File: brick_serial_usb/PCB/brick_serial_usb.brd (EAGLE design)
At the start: 27.9 x 39.4 mm, 18 parts, among them IC2 FT232RLSSOP

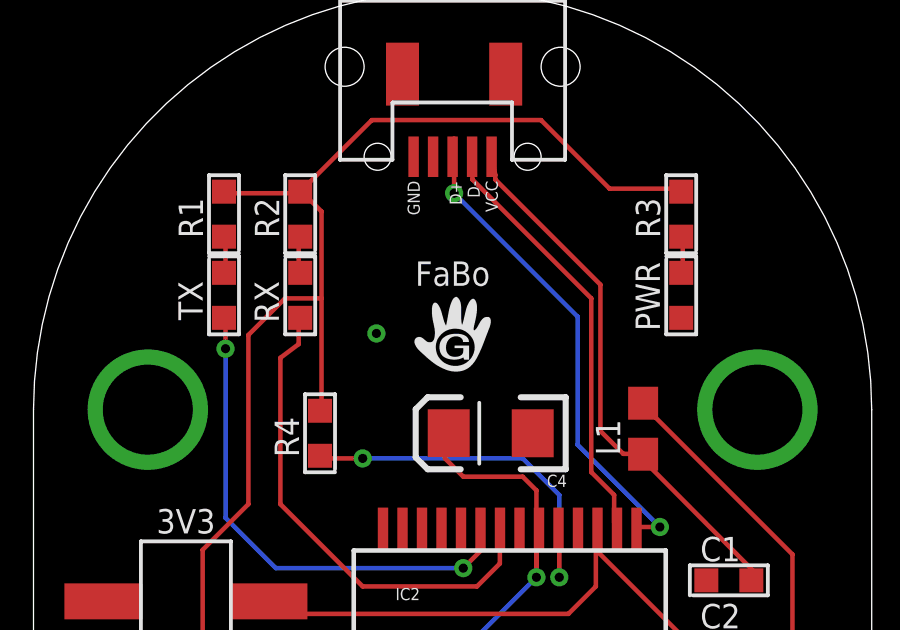
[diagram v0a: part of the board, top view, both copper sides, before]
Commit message: change logo
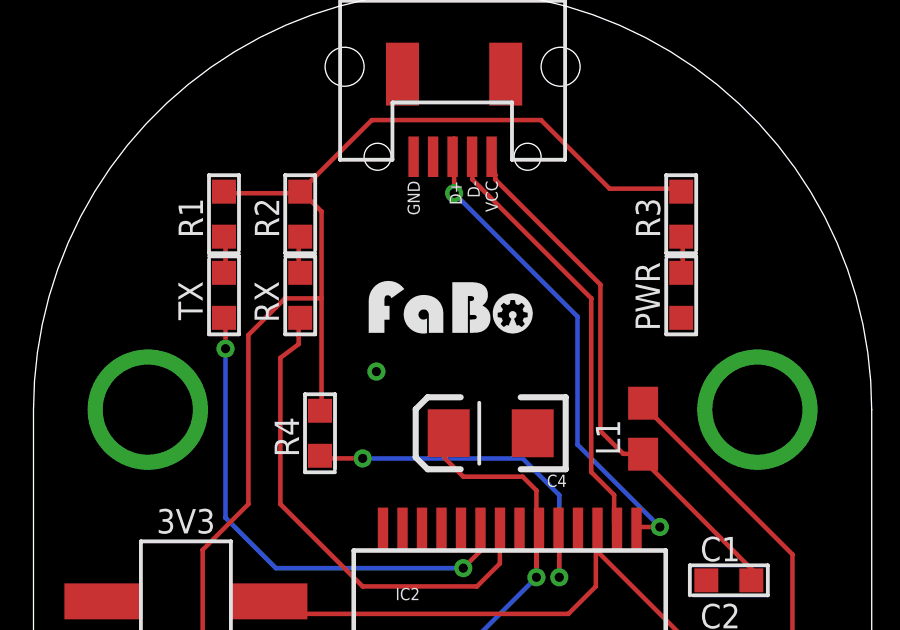
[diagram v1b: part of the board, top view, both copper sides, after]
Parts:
- removed U$4: A4L-LOC-FABO_S, gclue:LOGO_FABO_S
- added U$6: (no value), FaBo:LOGO_FABO_S
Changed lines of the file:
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@@
 <attribute name="NAME" x="22.225" y="15.875" size="0.8128" layer="25" font="vector"/>
 </element>
-<element name="U$4" library="gclue" package="LOGO_FABO_S" value="A4L-LOC-FABO_S" x="13.97" y="27.94"/>
 <element name="U$5" library="gclue" package="LOGO_OSHW_T_S" value="" x="3.81" y="8.89"/>
+<element name="U$6" library="FaBo" package="LOGO_FABO_S" value="" x="13.97" y="27.94"/>
 </elements>
 <signals>
@@
 <vertex x="-1.27" y="40.64"/>
 </polygon>
-<via x="11.43" y="27.94" extent="1-16" drill="0.3048"/>
+<via x="11.43" y="26.67" extent="1-16" drill="0.3048"/>
 </signal>
 <signal name="VCC">

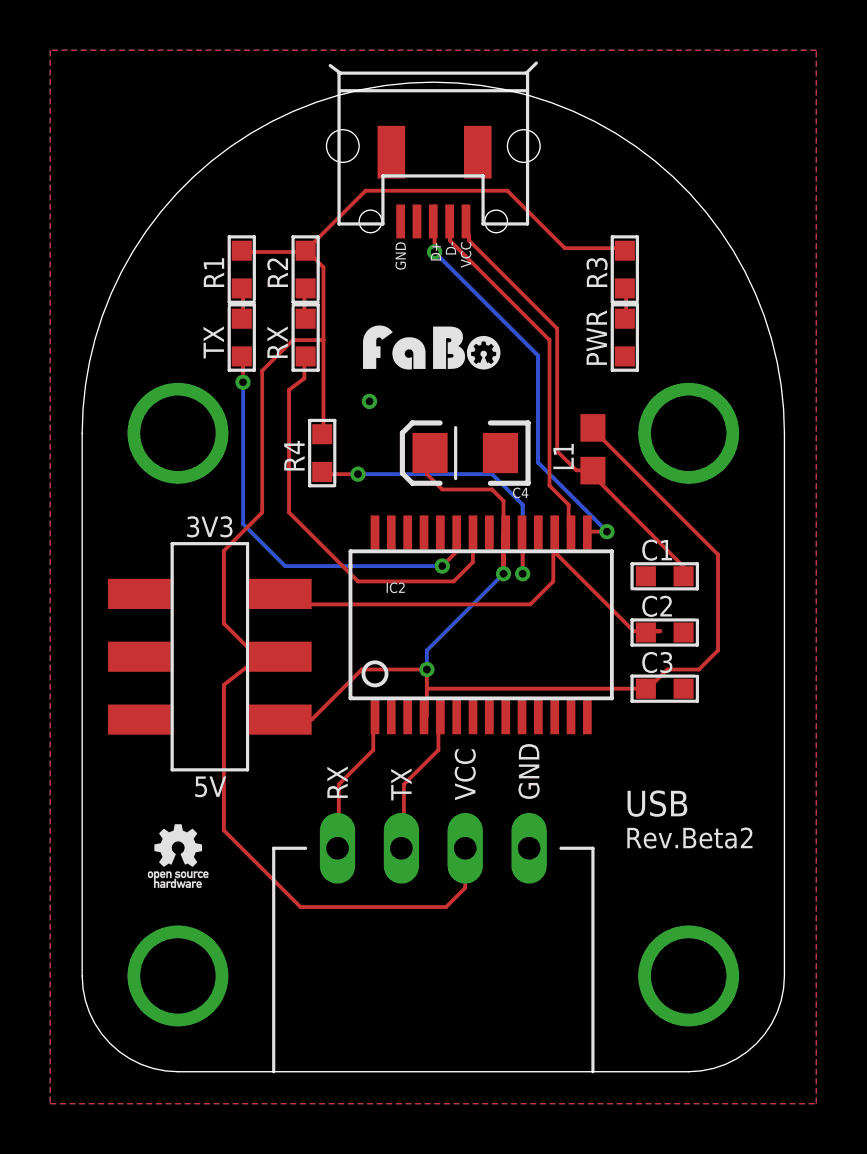
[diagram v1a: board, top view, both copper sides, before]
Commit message: add made-in-japan logo
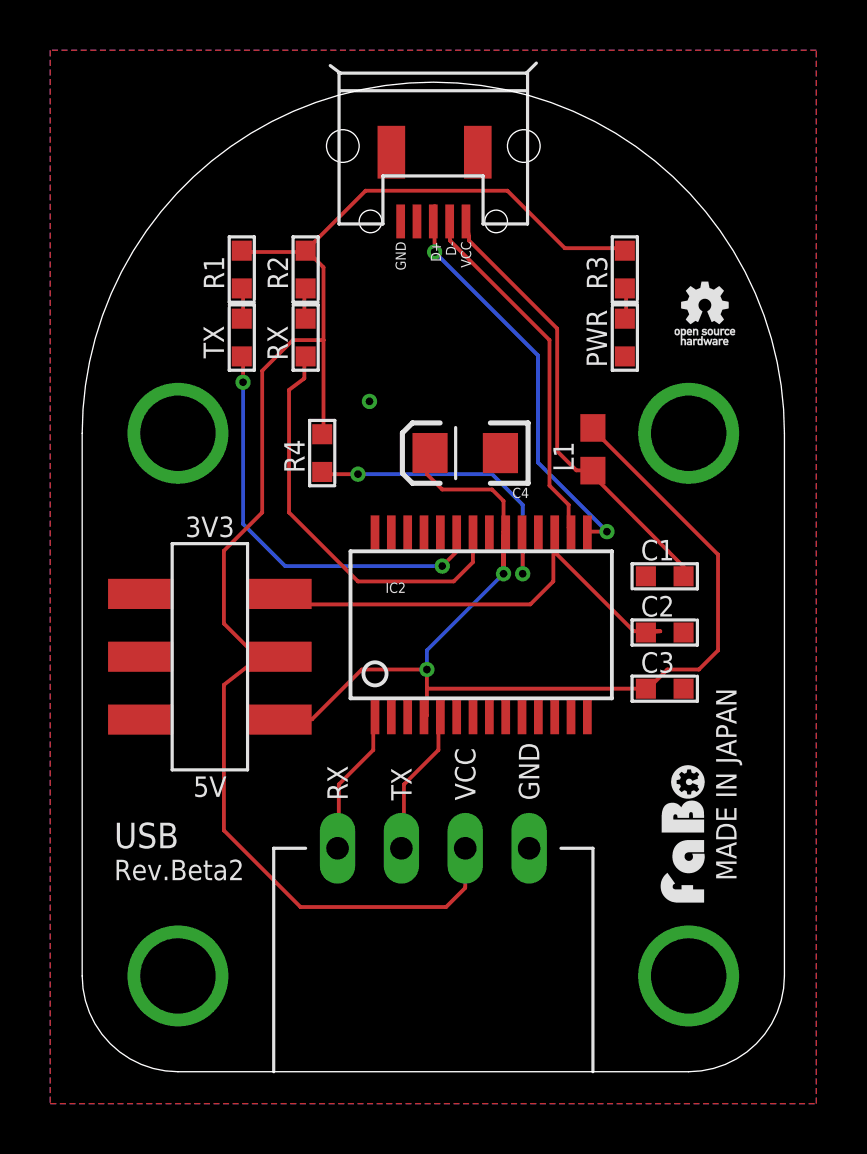
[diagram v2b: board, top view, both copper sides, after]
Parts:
- moved U$5 30.1 mm to (24.8, 30.5)
- moved U$6 21.3 mm to (24.8, 9.53), turned to 90 degrees
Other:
- board text added: "MADE IN JAPAN"
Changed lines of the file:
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@@
 <text x="5.08" y="11.7475" size="0.8128" layer="21" font="vector" align="top-center">5V</text>
 <text x="5.08" y="21.2725" size="0.8128" layer="21" font="vector" align="bottom-center">3V3</text>
-<text x="21.59" y="10.16" size="1.016" layer="21" font="vector">USB</text>
-<text x="21.59" y="8.89" size="0.8128" layer="21" font="vector">Rev.Beta2</text>
+<text x="1.27" y="8.89" size="1.016" layer="21" font="vector">USB</text>
+<text x="1.27" y="7.62" size="0.8128" layer="21" font="vector">Rev.Beta2</text>
+<text x="26.035" y="11.43" size="0.8128" layer="21" font="vector" rot="R90" align="bottom-center">MADE IN JAPAN</text>
 </plain>
 <attributes>
@@
 <attribute name="NAME" x="22.225" y="15.875" size="0.8128" layer="25" font="vector"/>
 </element>
-<element name="U$5" library="gclue" package="LOGO_OSHW_T_S" value="" x="3.81" y="8.89"/>
-<element name="U$6" library="FaBo" package="LOGO_FABO_S" value="" x="13.97" y="27.94"/>
+<element name="U$5" library="gclue" package="LOGO_OSHW_T_S" value="" x="24.765" y="30.48"/>
+<element name="U$6" library="FaBo" package="LOGO_FABO_S" value="" x="24.765" y="9.525" rot="R90"/>
 </elements>
 <signals>

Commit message: Update rev.1.0
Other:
- board text added: "Rev.1.0"
- board text removed: "Rev.Beta2"
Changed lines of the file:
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@@
 <text x="5.08" y="21.2725" size="0.8128" layer="21" font="vector" align="bottom-center">3V3</text>
 <text x="1.27" y="8.89" size="1.016" layer="21" font="vector">USB</text>
-<text x="1.27" y="7.62" size="0.8128" layer="21" font="vector">Rev.Beta2</text>
+<text x="1.27" y="7.62" size="0.8128" layer="21" font="vector">Rev.1.0</text>
 <text x="26.035" y="11.43" size="0.8128" layer="21" font="vector" rot="R90" align="bottom-center">MADE IN JAPAN</text>
 </plain>

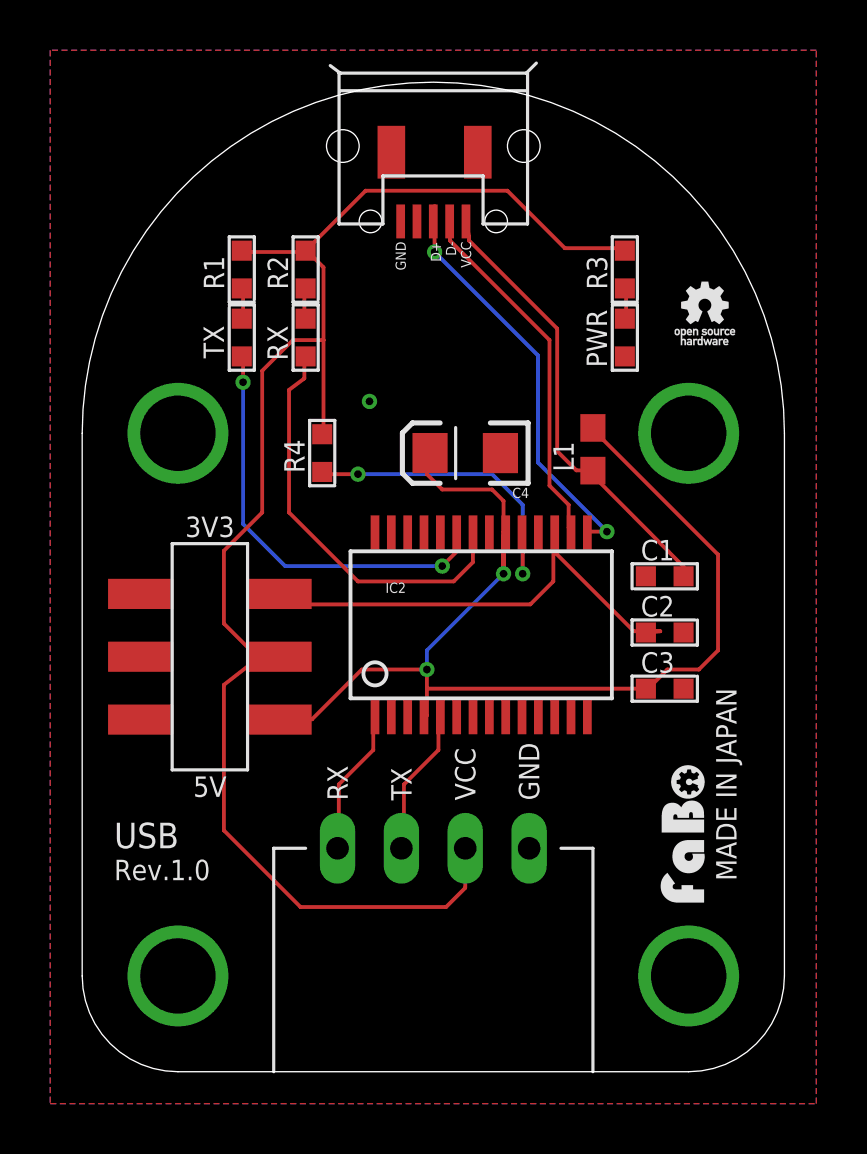
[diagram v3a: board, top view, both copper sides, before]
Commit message: change vcc level  brick_serial_ble_BLE113 refine board  brick_serial_usb
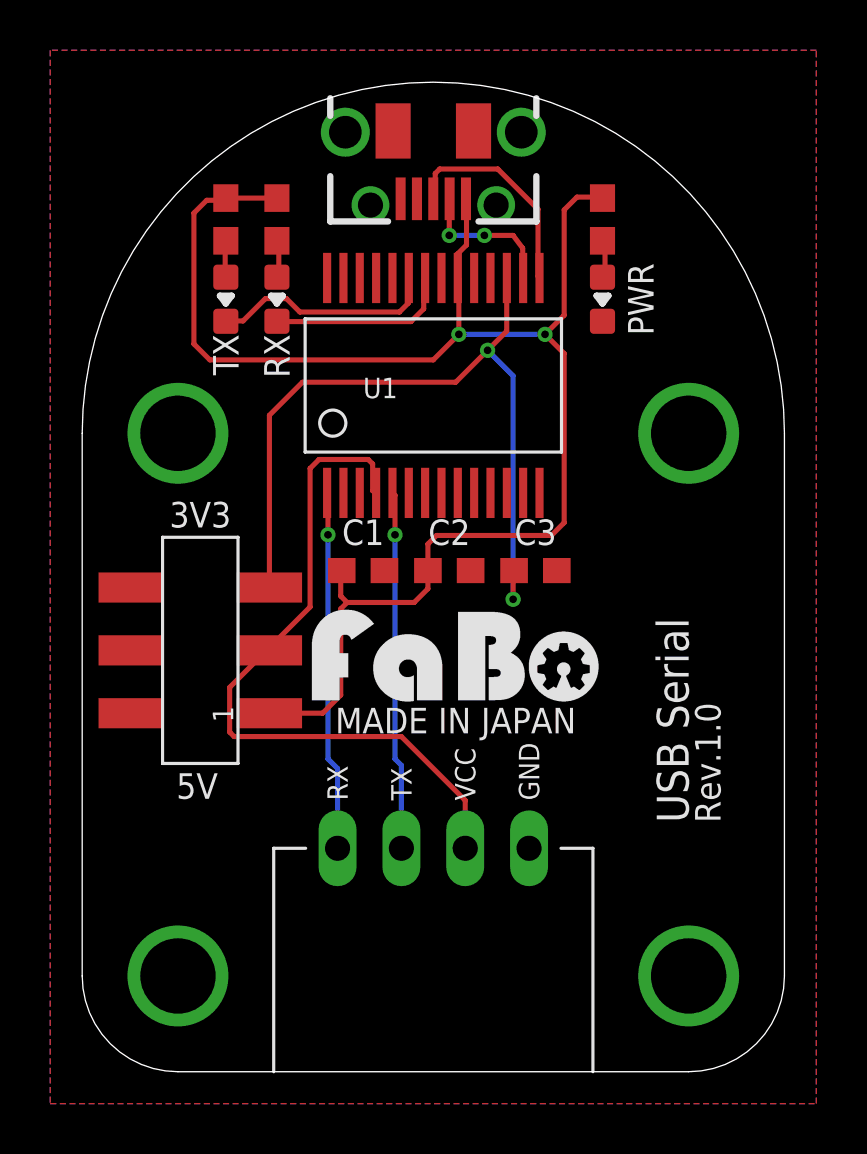
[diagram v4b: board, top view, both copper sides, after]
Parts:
- removed C4: 10μF, SparkFun:EIA3216
- removed IC2: FT232RLSSOP, SparkFun:SSOP28DB
- removed L1: (no value), SparkFun:0603
- removed R4: 4.7K, GClue-Resistors:0603
- removed U$1: USB-MICRO-B-FEMALE, gclue:USB-MICRO-B-FEMALE
- removed U$2: (no value), gclueParts:C&K_JS202011SCQN
- added JP1: USB-B-MICRO_SMD, gclue:USB_B_MICRO
- added SW1: (no value), gclue:C&K_JS202011SCQN
- added U1: FT232RL-SSOP28, gclue:SSOP28
- C1: value 10uf -> 0.1uF; device GClue-Capacitor:0603 -> gclue:EIA0603
- C2: value 0.1uf -> 10uF; device GClue-Capacitor:0603 -> gclue:EIA0603
- C3: value 0.1uf -> 0.1uF; device GClue-Capacitor:0603 -> gclue:EIA0603
- PWR, RX, TX: value LED0603 -> (none); device GClue-LED:0603 -> gclue:EIA0603-LED
- R1, R2, R3: value 270 -> (none); device GClue-Resistors:0603 -> gclue:EIA0603
- U$5: device gclue:LOGO_OSHW_T_S -> FaBo:LOGO_FABO_M
- U$6: device FaBo:LOGO_FABO_S -> gclue:LOGO_OSHW_T_M_BOTTOM
- moved U$5 18.6 mm to (14.9, 14.7)
- moved R1 14.5 mm to (20.7, 33.9)
- moved R3 14.0 mm to (7.75, 33.9)
- moved C1 12.0 mm to (11.2, 19.9)
- moved U$6 11.6 mm to (14.0, 5.33), turned to 0 degrees
- moved C2 8.92 mm to (14.6, 19.9), turned to 0 degrees
- moved C3 6.97 mm to (18.0, 19.9), turned to 0 degrees
- moved R2 3.75 mm to (5.71, 33.9)
- moved RX 1.91 mm to (7.75, 30.7), turned to 180 degrees
- moved PWR 1.76 mm to (20.7, 30.7), turned to 180 degrees
- moved TX 1.65 mm to (5.71, 30.7), turned to 180 degrees
- renumbered U$3 to J1
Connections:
- removed net +3V3: C2.2, IC2.17, U$2.3
- removed net +5V: C3.2, C4.A, IC2.20, IC2.4, L1.2, U$2.1
- removed net CTS: IC2.11
- removed net D+: IC2.15, U$1.D+
- removed net D-: IC2.16, U$1.D-
- removed net DCD: IC2.10
- removed net DSR: IC2.9
- removed net DTR: IC2.2
- removed net N$6: PWR.ANODE, R3.1
- removed net PWREN: IC2.14
- removed net RESET: IC2.19, R4.1
- removed net RI: IC2.6
- removed net RTS: IC2.3
- removed net SLEEP: IC2.12
- removed net TXDEN: IC2.13
- new net 3V3: C3.1, SW1.3, U1.17
- new net 5V: C1.1, C2.1, JP1.VBUS, R1.2, R2.2, R3.2, SW1.1, U1.20
- new net N$3: R3.1, RX.A
- new net N$4: JP1.D-, U1.16
- net GND: now also C1.2, C2.2, C3.2, JP1.GND, PWR.C, U1.18, U1.21, U1.25, U1.26, U1.7; no longer C1.1, C2.1, C3.1, C4.C, IC2.18, IC2.21, IC2.25, IC2.26, IC2.7, PWR.CATHODE, U$1.GND, U$1.GND1, U$1.GND2
- net N$1: now also PWR.A, R1.1; no longer C1.2, L1.1, U$1.VCC
- net N$2: now also R2.1, TX.A; no longer R1.1, TX.ANODE
- net N$5: now also JP1.D+, U1.15; no longer R2.1, RX.ANODE
- net RX: now also J1.RX, U1.1; no longer IC2.5, J1.TX
- net RXLED: now also RX.C, U1.22; no longer IC2.22, RX.CATHODE
- net TX: now also J1.TX, U1.5; no longer IC2.1, J1.RX
- net TXLED: now also TX.C, U1.23; no longer IC2.23, TX.CATHODE
- net VCC: now also SW1.2, U1.4; no longer R1.2, R2.2, R3.2, R4.2, U$2.2
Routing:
- net 5V: track 0.00 -> 63.1 mm, vias 0 -> 2
- net +5V: track 47.8 -> 0.00 mm, vias 2 -> 0
- net VCC: track 61.6 -> 28.2 mm
- net 3V3: track 0.00 -> 31.3 mm, vias 0 -> 2
- net +3V3: track 19.5 -> 0.00 mm
- net N$1: track 18.5 -> 1.55 mm
- net D+: track 16.7 -> 0.00 mm, vias 2 -> 0
- net D-: track 14.4 -> 0.00 mm
- net RESET: track 12.9 -> 0.00 mm, vias 2 -> 0
- net RXLED: track 16.5 -> 7.30 mm
- net TX: track 5.83 -> 14.3 mm, vias 0 -> 1
- net RX: track 5.88 -> 14.3 mm, vias 0 -> 1
- net TXLED: track 16.9 -> 9.00 mm, vias 2 -> 0
- net N$5: track 1.24 -> 8.61 mm
- net N$4: track 0.00 -> 5.82 mm, vias 0 -> 2
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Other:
- board text added: "USB Serial"
- board text removed: "USB"

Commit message: change brick_serial_usb
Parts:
- J1: device gclue:BRICK_SERIAL -> FaBo-etc:BRICK_SERIAL
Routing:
- net 3V3: track 31.3 -> 30.4 mm
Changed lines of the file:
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@@
 </autorouter>
 <elements>
-<element name="J1" library="gclue" package="BRICK_SERIAL" value="" x="13.97" y="19.05"/>
 <element name="U1" library="gclue" package="SSOP28" value="FT232RL-SSOP28" x="13.97" y="27.305" smashed="yes">
 <attribute name="NAME" x="11.176" y="26.797" size="0.8128" layer="25" font="vector"/>
@@
 <element name="U$5" library="FaBo" package="LOGO_FABO_M" value="" x="14.859" y="14.732"/>
 <element name="U$6" library="gclue" package="LOGO_OSHW_T_M_BOTTOM" value="" x="13.97" y="5.334"/>
+<element name="J1" library="FaBo-etc" package="BRICK_SERIAL" value="" x="13.97" y="19.05"/>
 </elements>
 <signals>
@@
 <contactref element="C2" pad="2"/>
 <contactref element="JP1" pad="GND"/>
-<contactref element="J1" pad="GND"/>
 <contactref element="PWR" pad="C"/>
 <polygon width="0.2032" layer="16" spacing="0.1524">
@@
 <vertex x="-1.27" y="40.64"/>
 </polygon>
+<contactref element="J1" pad="GND"/>
 </signal>
 <signal name="5V">
@@
 <contactref element="C3" pad="1"/>
 <contactref element="SW1" pad="3"/>
-<wire x1="7.449" y1="19.264" x2="7.449" y2="26.118" width="0.2032" layer="1"/>
-<wire x1="7.449" y1="26.118" x2="8.763" y2="27.432" width="0.2032" layer="1"/>
-<wire x1="8.763" y1="27.432" x2="14.859" y2="27.432" width="0.2032" layer="1"/>
-<wire x1="14.859" y1="27.432" x2="16.0655" y2="28.6385" width="0.2032" layer="1"/>
-<wire x1="16.129" y1="28.702" x2="16.891" y2="29.464" width="0.2032" layer="1"/>
-<wire x1="16.891" y1="29.464" x2="16.891" y2="31.576" width="0.2032" layer="1"/>
+<wire x1="7.449" y1="19.264" x2="7.449" y2="24.848" width="0.2032" layer="1"/>
+<wire x1="7.449" y1="24.848" x2="9.271" y2="26.67" width="0.2032" layer="1"/>
+<wire x1="9.271" y1="26.67" x2="15.621" y2="26.67" width="0.2032" layer="1"/>
+<wire x1="15.621" y1="26.67" x2="16.891" y2="27.94" width="0.2032" layer="1"/>
+<wire x1="16.891" y1="27.94" x2="16.891" y2="31.576" width="0.2032" layer="1"/>
 <wire x1="16.891" y1="31.576" x2="16.895" y2="31.58" width="0.2032" layer="1"/>
 <wire x1="17.184" y1="19.939" x2="17.184" y2="19.851" width="0.2032" layer="1"/>
@@
 <via x="17.145" y="18.796" extent="1-16" drill="0.3048"/>
 <wire x1="17.145" y1="18.796" x2="17.145" y2="27.686" width="0.2032" layer="16"/>
-<wire x1="17.145" y1="27.686" x2="16.129" y2="28.702" width="0.2032" layer="16"/>
-<via x="16.129" y="28.702" extent="1-16" drill="0.3048"/>
-<wire x1="16.129" y1="28.702" x2="16.0655" y2="28.6385" width="0.2032" layer="1"/>
+<wire x1="17.145" y1="27.686" x2="16.891" y2="27.94" width="0.2032" layer="16"/>
+<via x="16.891" y="27.94" extent="1-16" drill="0.3048"/>
 </signal>
 <signal name="VCC">
 <contactref element="U1" pad="4"/>
 <contactref element="SW1" pad="2"/>
-<contactref element="J1" pad="VCC"/>
 <wire x1="11.557" y1="24.1808" x2="11.557" y2="23.114" width="0.2032" layer="1"/>
 <wire x1="11.3792" y1="24.3586" x2="11.557" y2="24.1808" width="0.2032" layer="1"/>
@@
 <wire x1="5.8674" y1="15.2908" x2="5.8674" y2="13.5128" width="0.2032" layer="1"/>
 <wire x1="7.2898" y1="16.7132" x2="5.8674" y2="15.2908" width="0.2032" layer="1"/>
-<wire x1="15.24" y1="10.795" x2="15.24" y2="8.89" width="0.2032" layer="1"/>
 <wire x1="7.2898" y1="16.7132" x2="7.449" y2="16.764" width="0.2032" layer="1"/>
+<contactref element="J1" pad="VCC"/>
+<wire x1="15.24" y1="8.89" x2="15.24" y2="10.795" width="0.2032" layer="1"/>
 </signal>
 <signal name="RX">
 <contactref element="U1" pad="1"/>
+<wire x1="9.779" y1="21.3614" x2="9.779" y2="22.9362" width="0.2032" layer="1"/>
+<wire x1="9.779" y1="21.336" x2="9.779" y2="21.3614" width="0.2032" layer="16"/>
+<wire x1="10.16" y1="20.955" x2="9.779" y2="21.336" width="0.2032" layer="16"/>
+<wire x1="9.779" y1="22.9362" x2="9.745" y2="23.03" width="0.2032" layer="1"/>
+<via x="9.779" y="21.3614" extent="1-16" drill="0.3048"/>
 <contactref element="J1" pad="RX"/>
-<wire x1="9.779" y1="21.3614" x2="9.779" y2="22.9362" width="0.2032" layer="1"/>
-<wire x1="9.779" y1="12.446" x2="9.779" y2="21.3614" width="0.2032" layer="16"/>
-<wire x1="10.16" y1="12.065" x2="9.779" y2="12.446" width="0.2032" layer="16"/>
-<wire x1="9.779" y1="22.9362" x2="9.745" y2="23.03" width="0.2032" layer="1"/>
-<wire x1="10.16" y1="12.065" x2="10.16" y2="8.89" width="0.2032" layer="16"/>
-<via x="9.779" y="21.3614" extent="1-16" drill="0.3048"/>
+<wire x1="10.16" y1="8.89" x2="10.16" y2="20.955" width="0.2032" layer="16"/>
 </signal>
 <signal name="TX">
 <contactref element="U1" pad="5"/>
+<wire x1="12.446" y1="21.3614" x2="12.446" y2="22.9362" width="0.2032" layer="1"/>
+<wire x1="12.446" y1="21.336" x2="12.446" y2="21.3614" width="0.2032" layer="16"/>
+<wire x1="12.7" y1="21.082" x2="12.446" y2="21.336" width="0.2032" layer="16"/>
+<wire x1="12.446" y1="22.9362" x2="12.345" y2="23.03" width="0.2032" layer="1"/>
+<via x="12.446" y="21.3614" extent="1-16" drill="0.3048"/>
 <contactref element="J1" pad="TX"/>
-<wire x1="12.446" y1="21.3614" x2="12.446" y2="22.9362" width="0.2032" layer="1"/>
-<wire x1="12.446" y1="12.446" x2="12.446" y2="21.3614" width="0.2032" layer="16"/>
-<wire x1="12.7" y1="12.192" x2="12.446" y2="12.446" width="0.2032" layer="16"/>
-<wire x1="12.446" y1="22.9362" x2="12.345" y2="23.03" width="0.2032" layer="1"/>
-<wire x1="12.7" y1="12.192" x2="12.7" y2="8.89" width="0.2032" layer="16"/>
-<via x="12.446" y="21.3614" extent="1-16" drill="0.3048"/>
+<wire x1="12.7" y1="21.082" x2="12.7" y2="8.89" width="0.2032" layer="16"/>
 </signal>
 <signal name="N$1">
